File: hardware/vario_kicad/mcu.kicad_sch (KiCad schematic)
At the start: 19 parts, among them U5 STM32L072CBTx, Y1 Crystal, Y2 Crystal_GND24

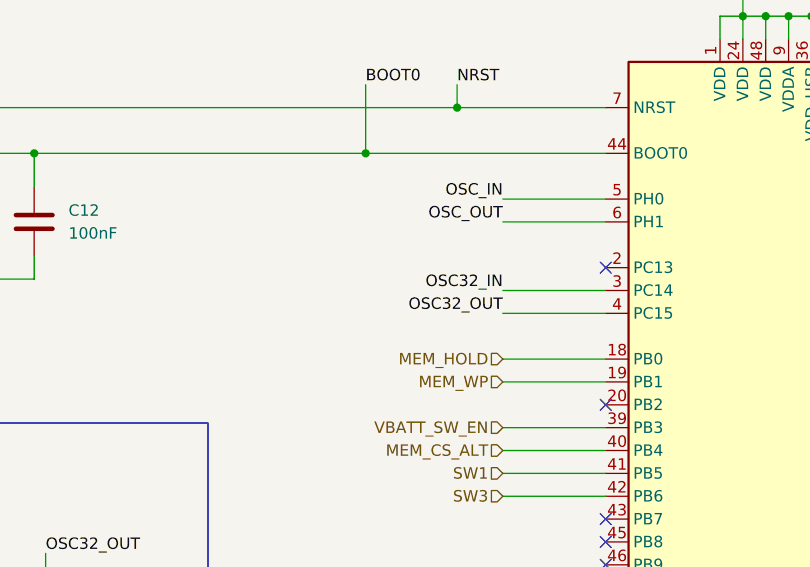
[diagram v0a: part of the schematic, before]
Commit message: add RTC_CALIB test point
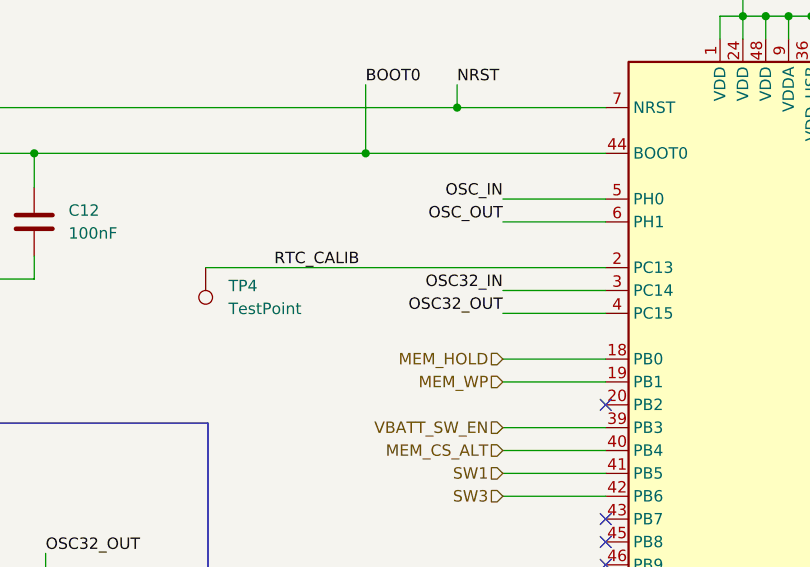
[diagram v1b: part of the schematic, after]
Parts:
- added TP4: TestPoint, symbol Connector:TestPoint
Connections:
- net RTC_CALIB: now reaches U5.2 (PC13)
- net RTC_CALIB: now also TP4.1
- no-connect marks 9 -> 8
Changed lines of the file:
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@@
 		(at 139.7 137.16)
 	)
-	(no_connect
-		(at 139.7 121.92)
-	)
 	(wire
 		(pts
@@
 	(wire
 		(pts
+			(xy 95.25 121.92) (xy 139.7 121.92)
+		)
+		(stroke
+			(width 0)
+			(type default)
+		)
+	)
+	(wire
+		(pts
 			(xy 265.43 93.98) (xy 265.43 97.79)
 		)
@@
 		)
 	)
+	(label "RTC_CALIB"
+		(at 102.87 121.92 0)
+		(effects
+			(font
+				(size 1.27 1.27)
+			)
+			(justify left bottom)
+		)
+	)
 	(label "OSC_IN"
 		(at 128.27 114.3 180)
@@
 					(unit 1)
 				)
+			)
+		)
+	)
+	(symbol
+		(lib_id "Connector:TestPoint")
+		(at 95.25 121.92 180)
+		(unit 1)
+		(exclude_from_sim no)
+		(in_bom yes)
+		(on_board yes)
+		(dnp no)
+		(fields_autoplaced yes)
+		(property "Reference" "TP4"
+			(at 97.79 123.9519 0)
+			(effects
+				(font
+					(size 1.27 1.27)
+				)
+				(justify right)
+			)
+		)
+		(property "Value" "TestPoint"
+			(at 97.79 126.4919 0)
+			(effects
+				(font
+					(size 1.27 1.27)
+				)
+				(justify right)
+			)
+		)
+		(property "Footprint" ""
+			(at 90.17 121.92 0)
+			(effects
+				(font
+					(size 1.27 1.27)
+				)
+				(hide yes)
+			)
+		)
+		(property "Datasheet" "~"
+			(at 90.17 121.92 0)
+			(effects
+				(font
+					(size 1.27 1.27)
+				)
+				(hide yes)
+			)
+		)
+		(property "Description" "test point"
+			(at 95.25 121.92 0)
+			(effects
+				(font
+					(size 1.27 1.27)
+				)
+				(hide yes)
+			)
+		)
+		(pin "1"
+		)
+		(instances
+			(project ""
+				(path "/50389aff-b244-451e-8e3a-c5addd2215e1/dd2cba4c-5ed6-4588-88fb-827c05b79647"
+					(reference "TP4")
+					(unit 1)
+				)

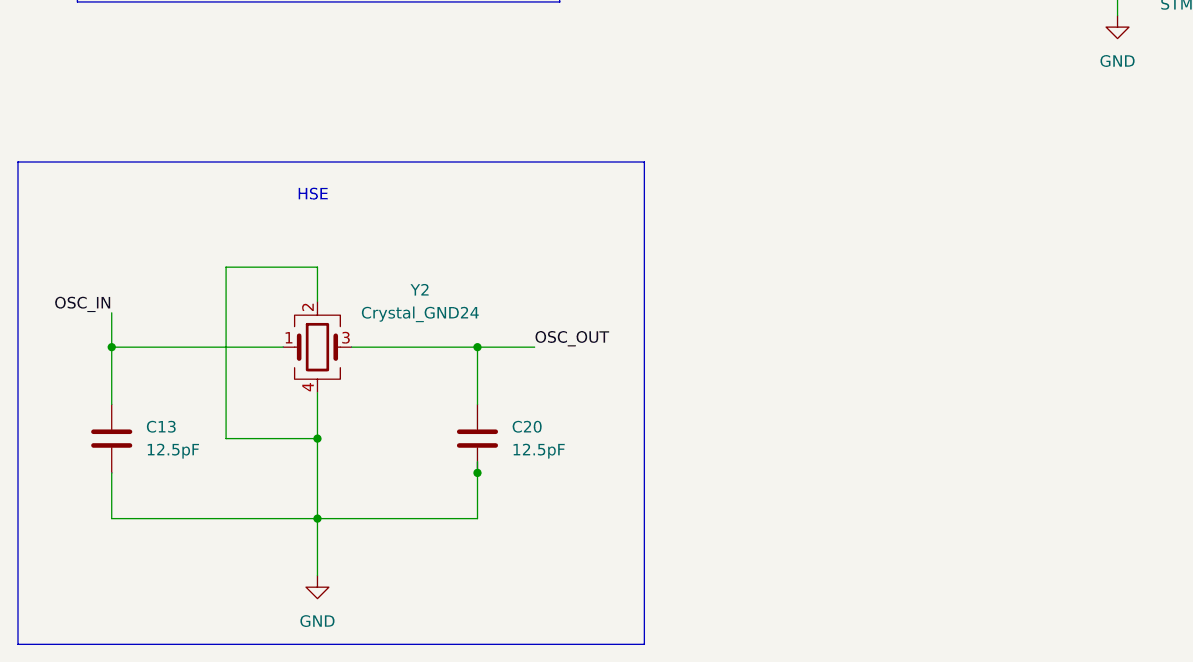
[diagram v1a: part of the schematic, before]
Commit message: add optional resistor for HSE oscillator
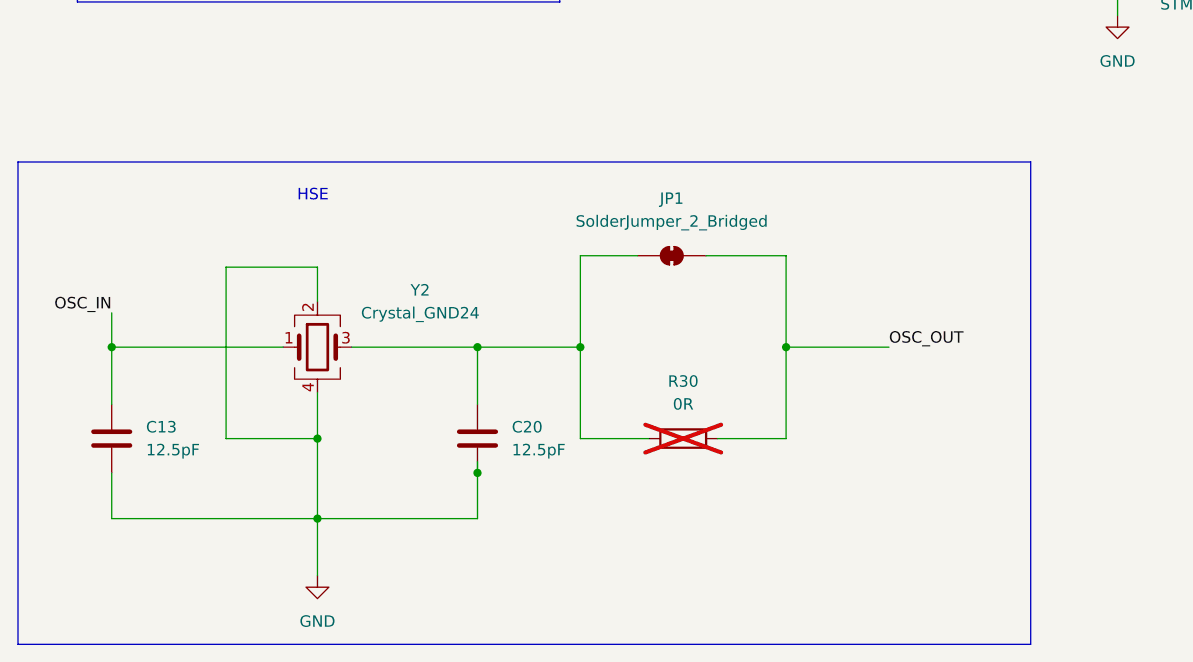
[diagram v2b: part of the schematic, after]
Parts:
- added JP1: SolderJumper_2_Bridged, Jumper:SolderJumper-2_P1.3mm_Open_TrianglePad1.0x1.5mm, symbol Jumper:SolderJumper_2_Bridged
- added R30: 0R, symbol Device:R
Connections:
- net OSC_OUT: now also JP1.2 (B), R30.2; no longer C20.1, Y2.3
- new net: C20.1, JP1.1 (A), R30.1, Y2.3
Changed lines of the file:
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@@
+	)
+	(junction
+		(at 97.79 218.44)
+		(diameter 0)
+		(color 0 0 0 0)
 	)
 	(junction
@@
 	(junction
 		(at 77.47 156.21)
+		(diameter 0)
+		(color 0 0 0 0)
+	)
+	(junction
+		(at 120.65 218.44)
 		(diameter 0)
 		(color 0 0 0 0)
@@
 	(wire
 		(pts
+			(xy 111.76 208.28) (xy 120.65 208.28)
+		)
+		(stroke
+			(width 0)
+			(type default)
+		)
+	)
+	(wire
+		(pts
 			(xy 58.42 171.45) (xy 68.58 171.45)
 		)
@@
 	(wire
 		(pts
+			(xy 120.65 208.28) (xy 120.65 218.44)
+		)
+		(stroke
+			(width 0)
+			(type default)
+		)
+	)
+	(wire
+		(pts
 			(xy 64.77 218.44) (xy 45.72 218.44)
 		)
@@
 	(wire
 		(pts
+			(xy 97.79 218.44) (xy 97.79 208.28)
+		)
+		(stroke
+			(width 0)
+			(type default)
+		)
+	)
+	(wire
+		(pts
 			(xy 240.03 105.41) (xy 240.03 107.95)
 		)
@@
 	(wire
 		(pts
+			(xy 120.65 218.44) (xy 120.65 228.6)
+		)
+		(stroke
+			(width 0)
+			(type default)
+		)
+	)
+	(wire
+		(pts
 			(xy 297.18 93.98) (xy 311.15 93.98)
 		)
@@
 	(wire
 		(pts
+			(xy 97.79 208.28) (xy 104.14 208.28)
+		)
+		(stroke
+			(width 0)
+			(type default)
+		)
+	)
+	(wire
+		(pts
 			(xy 175.26 104.14) (xy 182.88 104.14)
 		)
@@
 	(wire
 		(pts
+			(xy 97.79 228.6) (xy 105.41 228.6)
+		)
+		(stroke
+			(width 0)
+			(type default)
+		)
+	)
+	(wire
+		(pts
 			(xy 76.2 109.22) (xy 113.03 109.22)
 		)
@@
 	(wire
 		(pts
-			(xy 86.36 218.44) (xy 92.71 218.44)
+			(xy 86.36 218.44) (xy 97.79 218.44)
 		)
 		(stroke
@@
 	(wire
 		(pts
+			(xy 120.65 218.44) (xy 132.08 218.44)
+		)
+		(stroke
+			(width 0)
+			(type default)
+		)
+	)
+	(wire
+		(pts
 			(xy 154.94 91.44) (xy 154.94 93.98)
 		)
@@
 		(pts
 			(xy 175.26 106.68) (xy 182.88 106.68)
+		)
+		(stroke
+			(width 0)
+			(type default)
+		)
+	)
+	(wire
+		(pts
+			(xy 97.79 218.44) (xy 97.79 228.6)
+		)
+		(stroke
+			(width 0)
+			(type default)
+		)
+	)
+	(wire
+		(pts
+			(xy 120.65 228.6) (xy 113.03 228.6)
 		)
 		(stroke
@@
 	(rectangle
 		(start 35.306 197.866)
-		(end 104.902 251.46)
+		(end 147.828 251.46)
 		(stroke
 			(width 0)
@@
 		)
 	)
-	(label "OSC_OUT"
-		(at 92.71 218.44 0)
-		(effects
-			(font
-				(size 1.27 1.27)
-			)
-			(justify left bottom)
-		)
-	)
 	(label "SWDIO"
 		(at 182.88 137.16 0)
@@
 			)
 			(justify right bottom)
+		)
+	)
+	(label "OSC_OUT"
+		(at 132.08 218.44 0)
+		(effects
+			(font
+				(size 1.27 1.27)
+			)
+			(justify left bottom)
 		)
 	)
@@
 	)
 	(symbol
+		(lib_id "Device:R")
+		(at 109.22 228.6 90)
+		(unit 1)
+		(exclude_from_sim no)
+		(in_bom yes)
+		(on_board yes)
+		(dnp yes)
+		(fields_autoplaced yes)
+		(property "Reference" "R30"
+			(at 109.22 222.25 90)
+			(effects
+				(font
+					(size 1.27 1.27)
+				)
+			)
+		)
+		(property "Value" "0R"
+			(at 109.22 224.79 90)
+			(effects
+				(font
+					(size 1.27 1.27)
+				)
+			)
+		)
+		(property "Footprint" ""
+			(at 109.22 230.378 90)
+			(effects
+				(font
+					(size 1.27 1.27)
+				)
+				(hide yes)
+			)
+		)
+		(property "Datasheet" "~"
+			(at 109.22 228.6 0)
+			(effects
+				(font
+					(size 1.27 1.27)
+				)
+				(hide yes)
+			)
+		)
+		(property "Description" "Resistor"
+			(at 109.22 228.6 0)
+			(effects
+				(font
+					(size 1.27 1.27)
+				)
+				(hide yes)
+			)
+		)
+		(pin "1"
+		)
+		(pin "2"
+		)
+		(instances
+			(project ""
+				(path "/50389aff-b244-451e-8e3a-c5addd2215e1/dd2cba4c-5ed6-4588-88fb-827c05b79647"
+					(reference "R30")
+					(unit 1)
+				)
+			)
+		)
+	)
+	(symbol
 		(lib_id "power:VCC")
 		(at 154.94 91.44 0)
@@
 					(unit 1)
 				)
+			)
+		)
+	)
+	(symbol
+		(lib_id "Jumper:SolderJumper_2_Bridged")
+		(at 107.95 208.28 0)
+		(unit 1)
+		(exclude_from_sim yes)
+		(in_bom no)
+		(on_board yes)
+		(dnp no)
+		(fields_autoplaced yes)
+		(property "Reference" "JP1"
+			(at 107.95 201.93 0)
+			(effects
+				(font
+					(size 1.27 1.27)
+				)
+			)
+		)
+		(property "Value" "SolderJumper_2_Bridged"
+			(at 107.95 204.47 0)
+			(effects
+				(font
+					(size 1.27 1.27)
+				)
+			)
+		)
+		(property "Footprint" "Jumper:SolderJumper-2_P1.3mm_Open_TrianglePad1.0x1.5mm"
+			(at 107.95 208.28 0)
+			(effects
+				(font
+					(size 1.27 1.27)
+				)
+				(hide yes)
+			)
+		)
+		(property "Datasheet" "~"
+			(at 107.95 208.28 0)
+			(effects
+				(font
+					(size 1.27 1.27)
+				)
+				(hide yes)
+			)
+		)
+		(property "Description" "Solder Jumper, 2-pole, closed/bridged"
+			(at 107.95 208.28 0)
+			(effects
+				(font
+					(size 1.27 1.27)
+				)
+				(hide yes)
+			)
+		)
+		(pin "1"
+		)
+		(pin "2"
+		)
+		(instances
+			(project ""
+				(path "/50389aff-b244-451e-8e3a-c5addd2215e1/dd2cba4c-5ed6-4588-88fb-827c05b79647"
+					(reference "JP1")
+					(unit 1)
+				)

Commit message: minor changes
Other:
- moved on the sheet: J2, JP1
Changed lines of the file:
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@@
 	(wire
 		(pts
-			(xy 111.76 208.28) (xy 120.65 208.28)
+			(xy 113.03 208.28) (xy 120.65 208.28)
 		)
 		(stroke
@@
 	(wire
 		(pts
-			(xy 191.77 236.22) (xy 186.69 236.22)
+			(xy 270.51 153.67) (xy 265.43 153.67)
 		)
 		(stroke
@@
 	(wire
 		(pts
-			(xy 186.69 224.79) (xy 191.77 224.79)
+			(xy 265.43 142.24) (xy 270.51 142.24)
 		)
 		(stroke
@@
 	(wire
 		(pts
-			(xy 97.79 208.28) (xy 104.14 208.28)
+			(xy 97.79 208.28) (xy 105.41 208.28)
 		)
 		(stroke
@@
 	(wire
 		(pts
-			(xy 186.69 217.17) (xy 191.77 217.17)
+			(xy 265.43 134.62) (xy 270.51 134.62)
 		)
 		(stroke
@@
 	(wire
 		(pts
-			(xy 186.69 232.41) (xy 191.77 232.41)
+			(xy 265.43 149.86) (xy 270.51 149.86)
 		)
 		(stroke
@@
 	(wire
 		(pts
-			(xy 186.69 209.55) (xy 186.69 217.17)
+			(xy 265.43 127) (xy 265.43 134.62)
 		)
 		(stroke
@@
 	(wire
 		(pts
-			(xy 186.69 228.6) (xy 191.77 228.6)
+			(xy 265.43 146.05) (xy 270.51 146.05)
 		)
 		(stroke
@@
 	(wire
 		(pts
-			(xy 186.69 236.22) (xy 186.69 240.03)
+			(xy 265.43 153.67) (xy 265.43 157.48)
 		)
 		(stroke
@@
 	(wire
 		(pts
-			(xy 186.69 220.98) (xy 191.77 220.98)
+			(xy 265.43 138.43) (xy 270.51 138.43)
 		)
 		(stroke
@@
 	)
 	(label "SWDIO"
-		(at 186.69 220.98 180)
+		(at 265.43 138.43 180)
 		(effects
 			(font
@@
 	)
 	(label "NRST"
-		(at 186.69 228.6 180)
+		(at 265.43 146.05 180)
 		(effects
 			(font
@@
 	)
 	(label "BOOT0"
-		(at 186.69 232.41 180)
+		(at 265.43 149.86 180)
 		(effects
 			(font
@@
 	)
 	(label "SWCLK"
-		(at 186.69 224.79 180)
+		(at 265.43 142.24 180)
 		(effects
 			(font
@@
 	(symbol
 		(lib_id "power:VCC")
-		(at 186.69 209.55 0)
+		(at 265.43 127 0)
 		(unit 1)
 		(exclude_from_sim no)
@@
 		(fields_autoplaced yes)
 		(property "Reference" "#PWR30"
-			(at 186.69 213.36 0)
+			(at 265.43 130.81 0)
 			(effects
 				(font
@@
 		)
 		(property "Value" "VCC"
-			(at 186.69 204.47 0)
+			(at 265.43 121.92 0)
 			(effects
 				(font
@@
 		)
 		(property "Footprint" ""
-			(at 186.69 209.55 0)
+			(at 265.43 127 0)
 			(effects
 				(font
@@
 		)
 		(property "Datasheet" ""
-			(at 186.69 209.55 0)
+			(at 265.43 127 0)
 			(effects
 				(font
@@
 		)
 		(property "Description" "Power symbol creates a global label with name \"VCC\""
-			(at 186.69 209.55 0)
+			(at 265.43 127 0)
 			(effects
 				(font
@@
 	(symbol
 		(lib_id "Jumper:SolderJumper_2_Bridged")
-		(at 107.95 208.28 0)
+		(at 109.22 208.28 0)
 		(unit 1)
 		(exclude_from_sim yes)
@@
 		(fields_autoplaced yes)
 		(property "Reference" "JP1"
-			(at 107.95 201.93 0)
+			(at 109.22 201.93 0)
 			(effects
 				(font
@@
 		)
 		(property "Value" "SolderJumper_2_Bridged"
-			(at 107.95 204.47 0)
+			(at 109.22 204.47 0)
 			(effects
 				(font
@@
 		)
 		(property "Footprint" "Jumper:SolderJumper-2_P1.3mm_Open_TrianglePad1.0x1.5mm"
-			(at 107.95 208.28 0)
+			(at 109.22 208.28 0)
 			(effects
 				(font
@@
 		)
 		(property "Datasheet" "~"
-			(at 107.95 208.28 0)
+			(at 109.22 208.28 0)
 			(effects
 				(font
@@
 		)
 		(property "Description" "Solder Jumper, 2-pole, closed/bridged"
-			(at 107.95 208.28 0)
+			(at 109.22 208.28 0)
 			(effects
 				(font
@@
 	(symbol
 		(lib_id "power:GND")
-		(at 186.69 240.03 0)
+		(at 265.43 157.48 0)
 		(unit 1)
 		(exclude_from_sim no)
@@
 		(fields_autoplaced yes)
 		(property "Reference" "#PWR34"
-			(at 186.69 246.38 0)
+			(at 265.43 163.83 0)
 			(effects
 				(font
@@
 		)
 		(property "Value" "GND"
-			(at 186.69 245.11 0)
+			(at 265.43 162.56 0)
 			(effects
 				(font
@@
 		)
 		(property "Footprint" ""
-			(at 186.69 240.03 0)
+			(at 265.43 157.48 0)
 			(effects
 				(font
@@
 		)
 		(property "Datasheet" ""
-			(at 186.69 240.03 0)
+			(at 265.43 157.48 0)
 			(effects
 				(font
@@
 		)
 		(property "Description" "Power symbol creates a global label with name \"GND\" , ground"
-			(at 186.69 240.03 0)
+			(at 265.43 157.48 0)
 			(effects
 				(font
@@
 	(symbol
 		(lib_id "New_Library:SWD_PROGRAMMING")
-		(at 196.85 210.82 0)
+		(at 275.59 128.27 0)
 		(unit 1)
 		(exclude_from_sim no)
@@
 		(fields_autoplaced yes)
 		(property "Reference" "J2"
-			(at 207.01 226.6949 0)
+			(at 285.75 144.1449 0)
 			(effects
 				(font
@@
 		)
 		(property "Value" "~"
-			(at 196.85 210.82 0)
+			(at 275.59 128.27 0)
 			(effects
 				(font
@@
 		)
 		(property "Footprint" "symbol_lib:SWD_programming"
-			(at 196.85 210.82 0)
+			(at 275.59 128.27 0)
 			(effects
 				(font
@@
 		)
 		(property "Datasheet" ""
-			(at 196.85 210.82 0)
+			(at 275.59 128.27 0)
 			(effects
 				(font
@@
 		)
 		(property "Description" ""
-			(at 196.85 210.82 0)
+			(at 275.59 128.27 0)
 			(effects
 				(font
